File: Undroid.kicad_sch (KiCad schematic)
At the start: 36 parts, among them J1 AudioJack2, J2 JAE_SIM_Card_SF72S006, U1 ATSAME70J19A-AN, U2 AS4C256M16D3, U3 Allwinner-A13, U4 USR-C322

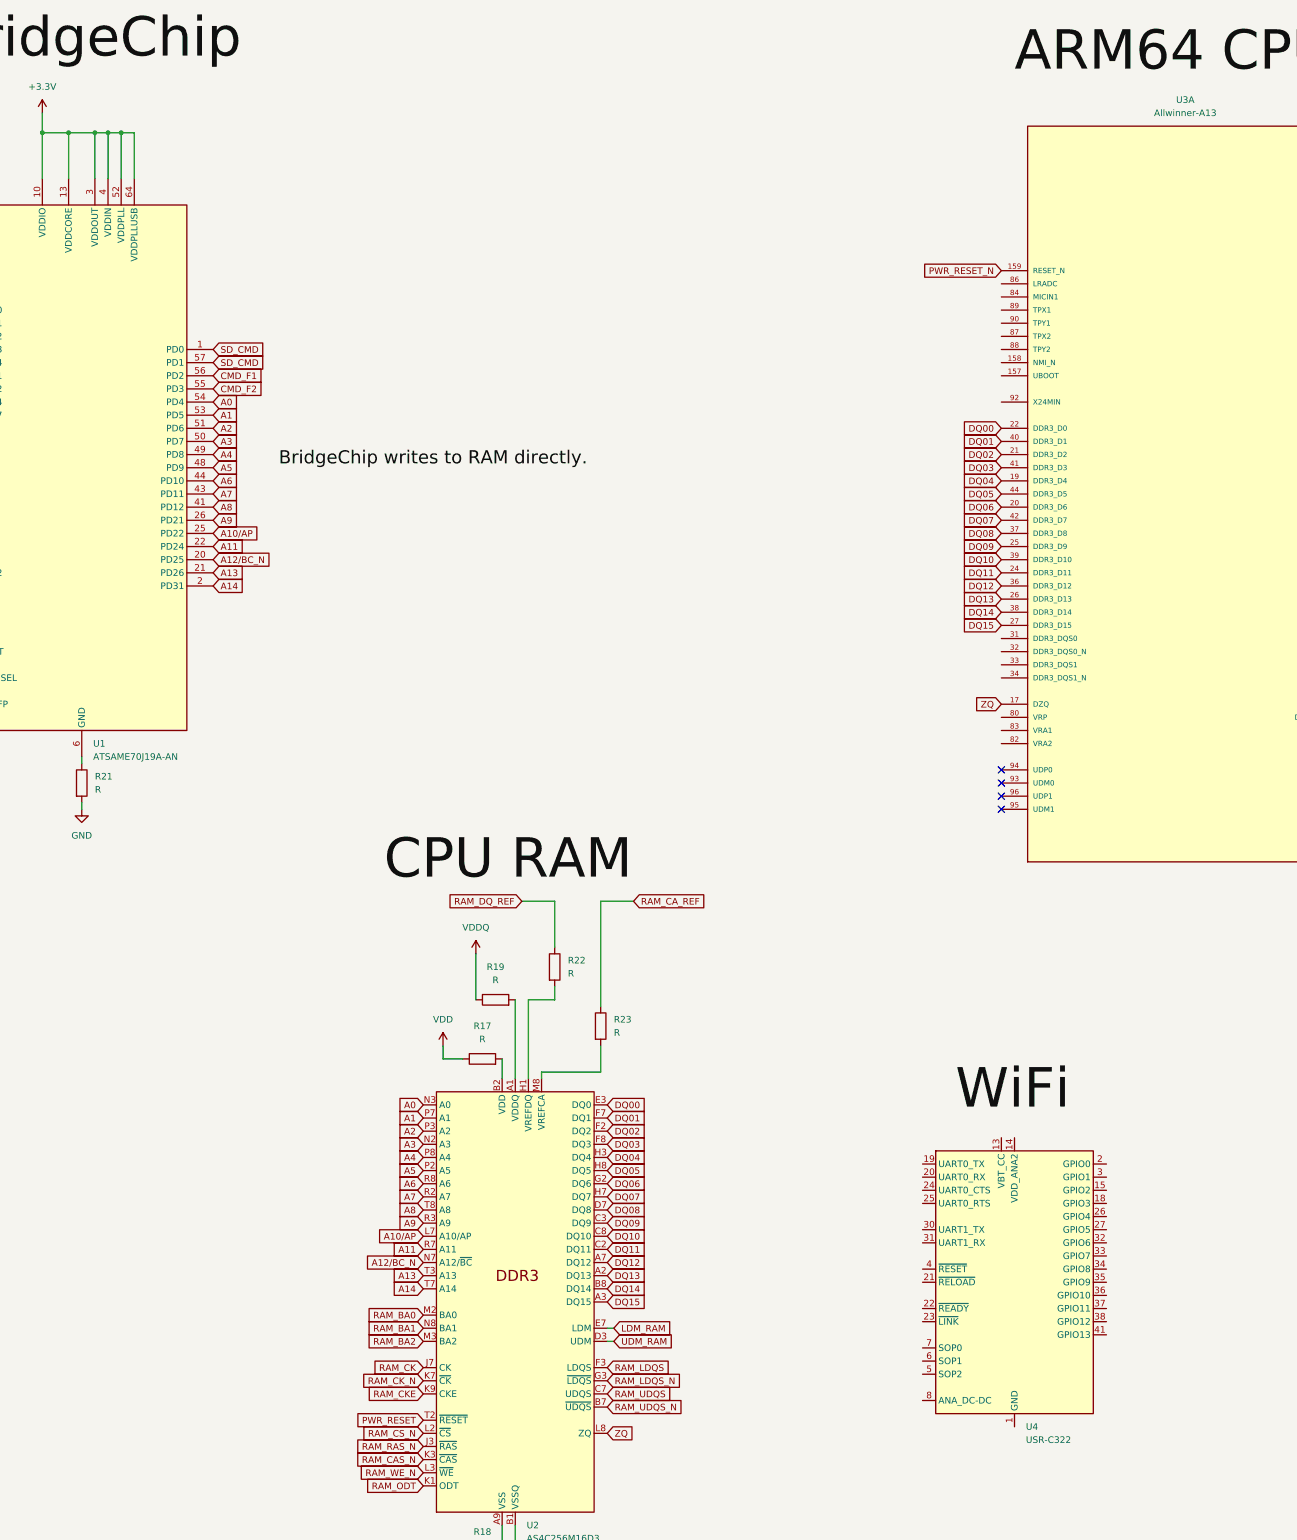
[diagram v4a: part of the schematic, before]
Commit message: main: Generate new pcb. Need to verify it.
Signed-off-by: Amlal EL Mahrouss <amlal@softwarelabs.com>
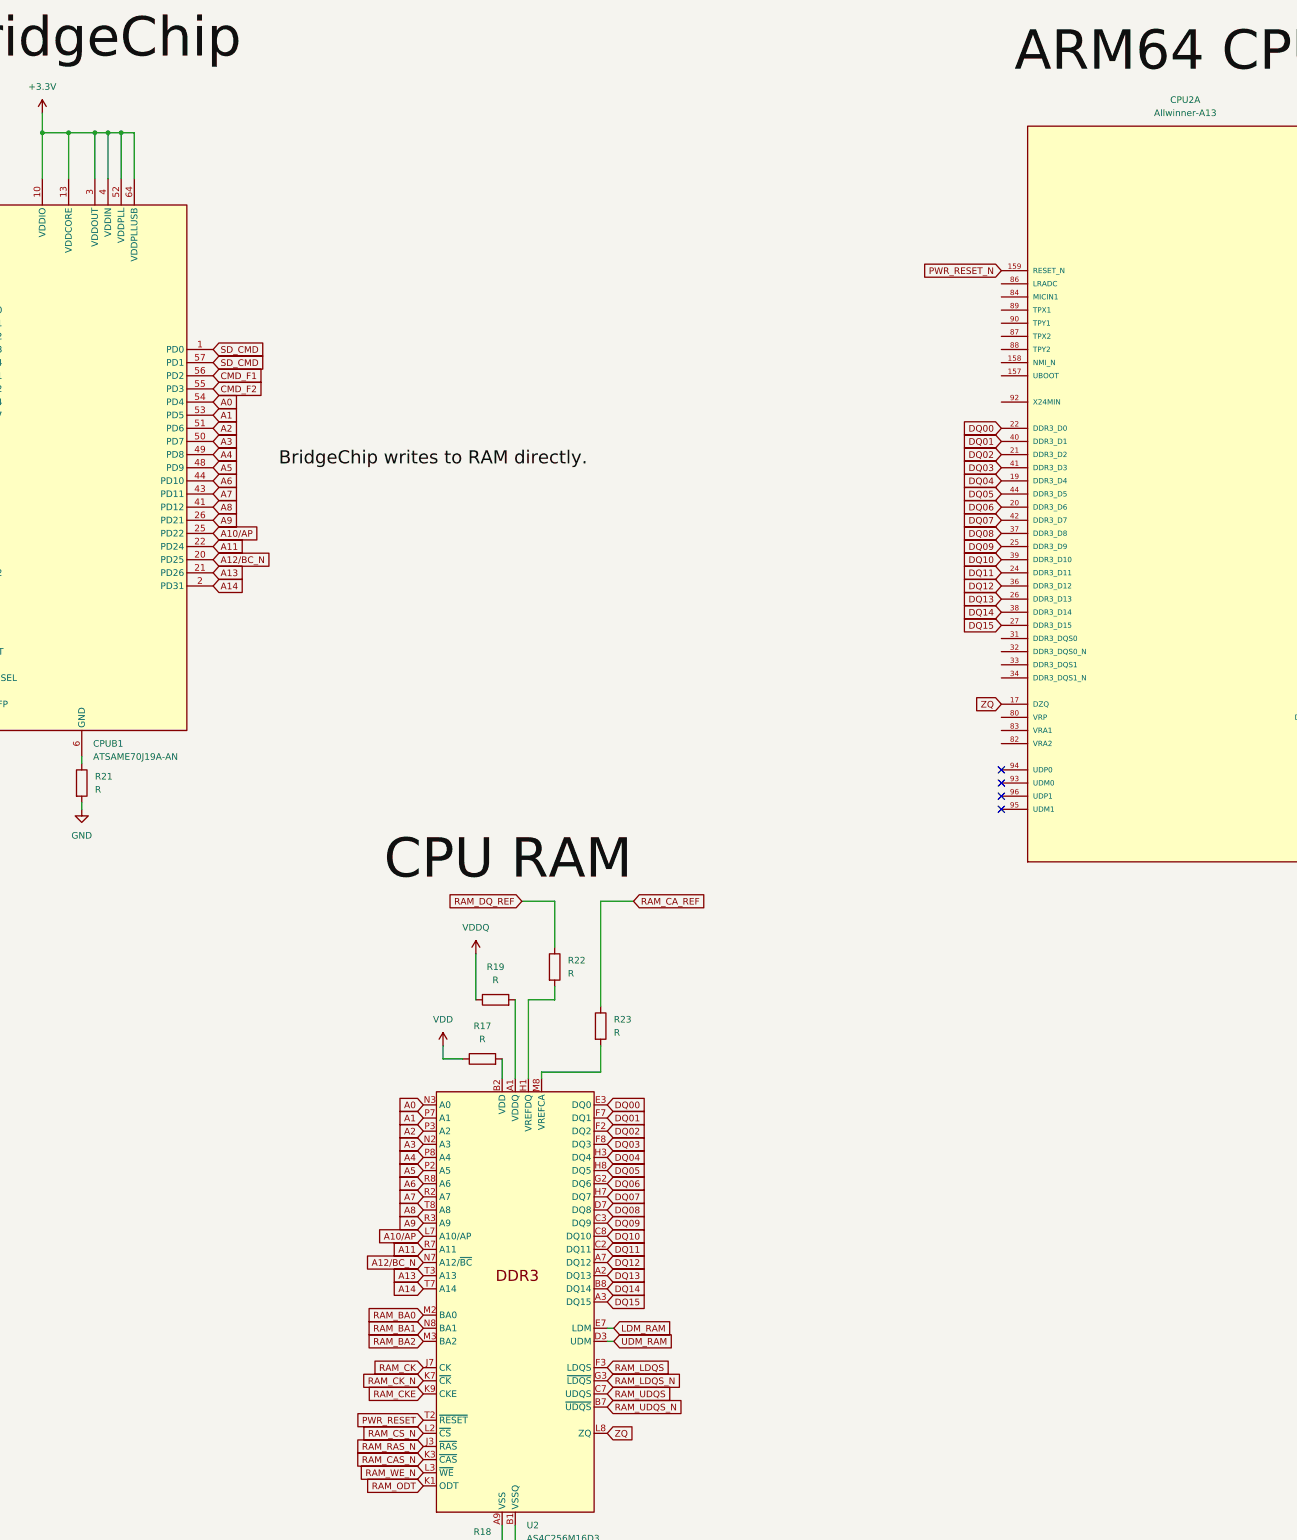
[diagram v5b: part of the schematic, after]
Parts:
- removed U4: USR-C322, RF_WiFi:USR-C322, symbol RF_WiFi:USR-C322
- CPU2: renamed from U3; footprint Allwinner-A13:QFP40P2200X2200X160-177N -> Allwinner:QFP40P2200X2200X160-177N
- renumbered U1 to CPUB1
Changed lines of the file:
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@@
 		)
 	)
-	(label "WiFi"
-		(at 463.55 278.13 0)
-		(fields_autoplaced yes)
-		(effects
-			(font
-				(size 7.62 7.62)
-			)
-			(justify left bottom)
-		)
-	)
 	(label "BridgeChip writes to RAM directly."
 		(at 332.74 152.4 0)
@@
 		(dnp no)
 		(fields_autoplaced yes)
-		(property "Reference" "U3"
+		(property "Reference" "CPU2"
 			(at 508 81.28 0)
 			(effects
@@
 			)
 		)
-		(property "Footprint" "Allwinner-A13:QFP40P2200X2200X160-177N"
+		(property "Footprint" "Allwinner:QFP40P2200X2200X160-177N"
 			(at 508 154.94 0)
 			(effects
@@
 			(project "Undroid"
 				(path "/5d3a3bfa-72d2-42b8-bac3-6ac6fe44d852"
-					(reference "U3")
+					(reference "CPU2")
 					(unit 1)
 				)
@@
 	)
 	(symbol
-		(lib_id "RF_WiFi:USR-C322")
-		(at 474.98 309.88 0)
-		(unit 1)
-		(exclude_from_sim no)
-		(in_bom yes)
-		(on_board yes)
-		(dnp no)
-		(fields_autoplaced yes)
-		(property "Reference" "U4"
-			(at 477.1741 337.82 0)
-			(effects
-				(font
-					(size 1.27 1.27)
-				)
-				(justify left)
-			)
-		)
-		(property "Value" "USR-C322"
-			(at 477.1741 340.36 0)
-			(effects
-				(font
-					(size 1.27 1.27)
-				)
-				(justify left)
-			)
-		)
-		(property "Footprint" "RF_WiFi:USR-C322"
-			(at 472.44 320.04 0)
-			(effects
-				(font
-					(size 1.27 1.27)
-				)
-				(hide yes)
-			)
-		)
-		(property "Datasheet" "https://www.usriot.com/download/WIFI/USR-C322%20User%20Manual%20V2.3.pdf"
-			(at 462.28 281.94 0)
-			(effects
-				(font
-					(size 1.27 1.27)
-				)
-				(hide yes)
-			)
-		)
-		(property "Description" "802.11 b/g/n Wi-Fi Module"
-			(at 474.98 309.88 0)
-			(effects
-				(font
-					(size 1.27 1.27)
-				)
-				(hide yes)
-			)
-		)
-		(pin "15"
-		)
-		(pin "16"
-		)
-		(pin "40"
-		)
-		(pin "13"
-		)
-		(pin "7"
-		)
-		(pin "22"
-		)
-		(pin "5"
-		)
-		(pin "1"
-		)
-		(pin "19"
-		)
-		(pin "11"
-		)
-		(pin "14"
-		)
-		(pin "17"
-		)
-		(pin "29"
-		)
-		(pin "28"
-		)
-		(pin "33"
-		)
-		(pin "38"
-		)
-		(pin "41"
-		)
-		(pin "8"
-		)
-		(pin "32"
-		)
-		(pin "26"
-		)
-		(pin "4"
-		)
-		(pin "21"
-		)
-		(pin "35"
-		)
-		(pin "31"
-		)
-		(pin "6"
-		)
-		(pin "42"
-		)
-		(pin "20"
-		)
-		(pin "12"
-		)
-		(pin "24"
-		)
-		(pin "39"
-		)
-		(pin "30"
-		)
-		(pin "25"
-		)
-		(pin "3"
-		)
-		(pin "10"
-		)
-		(pin "27"
-		)
-		(pin "34"
-		)
-		(pin "36"
-		)
-		(pin "44"
-		)
-		(pin "18"
-		)
-		(pin "23"
-		)
-		(pin "37"
-		)
-		(pin "43"
-		)
-		(pin "9"
-		)
-		(pin "2"
-		)
-		(instances
-			(project "Undroid"
-				(path "/5d3a3bfa-72d2-42b8-bac3-6ac6fe44d852"
-					(reference "U4")
-					(unit 1)
-				)
-			)
-		)
-	)
-	(symbol
 		(lib_id "Device:R")
 		(at 201.93 139.7 0)
@@
 		(dnp no)
 		(fields_autoplaced yes)
-		(property "Reference" "U1"
+		(property "Reference" "CPUB1"
 			(at 296.8341 205.74 0)
 			(effects
@@
 			(project "Undroid"
 				(path "/5d3a3bfa-72d2-42b8-bac3-6ac6fe44d852"
-					(reference "U1")
+					(reference "CPUB1")
 					(unit 1)
 				)

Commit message: main: new PCB.
Signed-off-by: Amlal EL Mahrouss <amlal@softwarelabs.com>
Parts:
- removed AE1: Antenna, RF_Antenna:Johanson_2450AT18x100, symbol Device:Antenna
- added AE1: Antenna_Shield, RF_Antenna:Texas_SWRA117D_2.4GHz_Right, symbol Device:Antenna_Shield
- added D1: LED, LED_SMD:LED_PLCC-2_3x2mm_AK, symbol Device:LED
- added J4: RFShield_OnePiece, RF_Shielding:Wuerth_36503205_20x20mm, symbol Device:RFShield_OnePiece
- added R10, R26, R27, R28, R29, R30, R31, R32: R, Resistor_SMD:R_0201_0603Metric, symbol Device:R
- renumbered PC1 to POWERC1
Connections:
- net CLK_F1 is gone; now on net RTC_OUT: FLASH1.3 (CLK)
- net CLK_F2 is gone; now on net RTC_OUT: FLASH2.3 (CLK)
- net +3.3V: now also CPU2.100 (VCC), CPU2.109 (VDD_INT), CPU2.11 (VDD_CPU), CPU2.142 (VCC), CPU2.149 (VDD_INT), CPU2.156 (VDD_CPU), CPU2.16 (VDD_CPU), CPU2.163 (VCC), CPU2.164 (VDD_CPU), CPU2.169 (VDD_CPU), CPU2.173 (VDD_CPU), CPU2.23 (VCC_DRAM), CPU2.30 (VCC_DRAM), CPU2.35 (VDD_INT), CPU2.4 (VDD_CPU), CPU2.43 (VCC_DRAM), CPU2.5 (VCC), CPU2.53 (VCC_DRAM), CPU2.62 (VCC_DRAM), CPU2.73 (VDD_INT), CPU2.81 (AVCC), CPU2.9 (VDD_CPU), CPU2.98 (VDD_INT), POWERC1.A9 (VBUS), POWERC1.B9 (VBUS); no longer R1.1
- net GND: now also CPU2.28 (DDR3_DM1), CPU2.29 (DDR3_DM0), CPU2.31 (DDR3_DQS0), CPU2.32 (DDR3_DQS0_N), CPU2.33 (DDR3_DQS1), CPU2.34 (DDR3_DQS1_N), CPU2.80 (VRP), CPU2.82 (VRA2), CPU2.83 (VRA1), CPU2.84 (MICIN1), CPU2.86 (LRADC), CPU2.87 (TPX2), CPU2.88 (TPY2), CPU2.89 (TPX1), CPU2.90 (TPY1), CPU2.93 (UDM0), CPU2.94 (UDP0), CPU2.95 (UDM1), CPU2.96 (UDP1), G1.11 (RTC_GPIO0), G1.12 (RTC_EINT), G1.24 (USB_VBUS), G1.25 (USB_DP), G1.26 (USB_DM), D1.1 (K), R10.1, R26.1, R27.1, R28.1, R29.1, R30.1, R31.1, R32.1; no longer CPUB1.38 (PB12), R15.1
- net GSM_STATUS: now also CPUB1.38 (PB12)
- net PWR_RESET: no longer U2.T2 (~{RESET})
- net RAM_BA0: now also CPU2.63 (DDR3_BA0)
- net RAM_BA1: now also CPU2.49 (DDR3_BA1)
- net RAM_BA2: now also CPU2.61 (DDR3_BA2)
- net RAM_CAS_N: now also CPU2.58 (DDR3_RAS)
- net RAM_CK: now also CPU2.45 (DDR3_CK)
- net RAM_CKE: now also CPU2.47 (DDR3_CKE)
- net RAM_CK_N: now also CPU2.46 (DDR3_CK_N)
- net RAM_ODT: now also CPU2.72 (DDR3_ODT)
- net RAM_RAS_N: now also CPU2.59 (DDR3_CAS)
- net RAM_WE_N: now also CPU2.60 (DDR3_WE)
- net at G1.32 (ANT): now also AE1.1 (A)
- net UBOOT: now reaches CPU2.157 (UBOOT)
- net NMI: now reaches CPU2.158 (NMI_N)
- net at CPU2.177 (GND): now also R16.2
- net at CPU2.18 (SVREF): now also R29.2
- net RAM_RST: now reaches CPU2.70 (DDR3_RST)
- net RAM_RST: now also U2.T2 (~{RESET})
- net at CPU2.74 (HPOUTL): now also R28.2
- net at CPU2.75 (HPBP): now also R27.2
- net at CPU2.76 (V33_HP): now also R30.2
- net at CPU2.77 (HPCOM): now also R26.2
- net at CPU2.78 (HPOUTR): now also R24.2
- net at CPU2.79 (AGND): now also R15.2
- net at CPU2.85 (VMIC): now also R32.2
- net RTC_OUT: now reaches CPU2.91 (X24MOUT)
- net RTC_OUT: now also J2.C3 (CLK), SD1.5 (CLK)
- net RTC_IN: now reaches CPU2.92 (X24MIN)
- net RTC_IN: now also G1.16 (SIM_CLK)
- net at CPU2.97 (V33_USB): now also R31.2
- net at POWERC1.A5 (CC1): now also R10.2; no longer R16.2
- net at POWERC1.B5 (CC2): now also R3.2; no longer R15.2
- net SHIELD: now reaches POWERC1.S1 (SHIELD)
- net SHIELD: now also SD1.9 (SHIELD), AE1.2 (Shield), J4.1 (Shield); no longer R3.2
- removed net GSM_CLK: G1.16 (SIM_CLK), J2.C3 (CLK), SD1.5 (CLK)
- net GSM_NET_LIGHT: no longer names the net of G1.41 (NETLIGHT)
- net GSM_NET_LIGHT: now also R1.2
- net GSM_SH: no longer names the net of J2.SH
- net PWR_RESET_N renamed PWR_RESET_BUT
- new net: D1.2 (A), R1.1
- new net GNDA: R15.1
- no-connect marks 9 -> 0
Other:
- moved on the sheet: R4, R5

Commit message: main: Reworking board now, because of Allwinner QFP package.
Signed-off-by: Amlal EL Mahrouss <amlal@softwarelabs.com>
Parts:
- added SHIELD_WUERTH1, SHIELD_WUERTH2: RFShield_OnePiece, RF_Shielding:Wuerth_36503205_20x20mm, symbol Device:RFShield_OnePiece
- renumbered J4 to SHIELD_WUERTH3
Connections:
- net SHIELD: no longer POWERC1.S1 (SHIELD), SD1.9 (SHIELD)
- new net: SD1.9 (SHIELD), SHIELD_WUERTH1.1 (Shield)
- new net: POWERC1.S1 (SHIELD), SHIELD_WUERTH2.1 (Shield)
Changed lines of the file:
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@@
 	(wire
 		(pts
-			(xy 561.34 96.52) (xy 543.56 96.52)
+			(xy 562.61 96.52) (xy 543.56 96.52)
 		)
 		(stroke
@@
 	(wire
 		(pts
-			(xy 561.34 93.98) (xy 561.34 96.52)
+			(xy 562.61 93.98) (xy 562.61 96.52)
 		)
 		(stroke
@@
 		)
 	)
+	(label "For Antenna"
+		(at 262.89 325.12 0)
+		(fields_autoplaced yes)
+		(effects
+			(font
+				(size 2.54 2.54)
+			)
+			(justify left bottom)
+		)
+	)
 	(label "BridgeChip writes to RAM directly."
 		(at 332.74 152.4 0)
@@
 		)
 	)
-	(global_label "SHIELD"
-		(shape input)
-		(at 209.55 170.18 270)
-		(fields_autoplaced yes)
-		(effects
-			(font
-				(size 1.27 1.27)
-			)
-			(justify right)
-		)
-		(property "Intersheetrefs" "${INTERSHEET_REFS}"
-			(at 209.55 179.7571 90)
-			(effects
-				(font
-					(size 1.27 1.27)
-				)
-				(justify right)
-				(hide yes)
-			)
-		)
-	)
 	(global_label "SD0_F1"
 		(shape input)
@@
 		)
 	)
-	(global_label "SHIELD"
-		(shape input)
-		(at 215.9 309.88 270)
-		(fields_autoplaced yes)
-		(effects
-			(font
-				(size 1.27 1.27)
-			)
-			(justify right)
-		)
-		(property "Intersheetrefs" "${INTERSHEET_REFS}"
-			(at 215.9 319.4571 90)
-			(effects
-				(font
-					(size 1.27 1.27)
-				)
-				(justify right)
-				(hide yes)
-			)
-		)
-	)
 	(global_label "SD_DAT1"
 		(shape input)
@@
 	)
 	(symbol
+		(lib_id "Device:RFShield_OnePiece")
+		(at 215.9 320.04 180)
+		(unit 1)
+		(exclude_from_sim no)
+		(in_bom yes)
+		(on_board yes)
+		(dnp no)
+		(fields_autoplaced yes)
+		(property "Reference" "SHIELD_WUERTH1"
+			(at 232.41 318.7699 0)
+			(effects
+				(font
+					(size 1.27 1.27)
+				)
+				(justify right)
+			)
+		)
+		(property "Value" "RFShield_OnePiece"
+			(at 232.41 321.3099 0)
+			(effects
+				(font
+					(size 1.27 1.27)
+				)
+				(justify right)
+			)
+		)
+		(property "Footprint" "RF_Shielding:Wuerth_36503205_20x20mm"
+			(at 215.9 317.5 0)
+			(effects
+				(font
+					(size 1.27 1.27)
+				)
+				(hide yes)
+			)
+		)
+		(property "Datasheet" "~"
+			(at 215.9 317.5 0)
+			(effects
+				(font
+					(size 1.27 1.27)
+				)
+				(hide yes)
+			)
+		)
+		(property "Description" "One-piece EMI RF shielding cabinet"
+			(at 215.9 320.04 0)
+			(effects
+				(font
+					(size 1.27 1.27)
+				)
+				(hide yes)
+			)
+		)
+		(pin "1"
+		)
+		(instances
+			(project "Undroid"
+				(path "/5d3a3bfa-72d2-42b8-bac3-6ac6fe44d852"
+					(reference "SHIELD_WUERTH1")
+					(unit 1)
+				)
+			)
+		)
+	)
+	(symbol
 		(lib_id "Device:R")
 		(at 374.65 255.27 90)
@@
 	)
 	(symbol
+		(lib_id "Device:RFShield_OnePiece")
+		(at 209.55 180.34 180)
+		(unit 1)
+		(exclude_from_sim no)
+		(in_bom yes)
+		(on_board yes)
+		(dnp no)
+		(fields_autoplaced yes)
+		(property "Reference" "SHIELD_WUERTH2"
+			(at 226.06 179.0699 0)
+			(effects
+				(font
+					(size 1.27 1.27)
+				)
+				(justify right)
+			)
+		)
+		(property "Value" "RFShield_OnePiece"
+			(at 226.06 181.6099 0)
+			(effects
+				(font
+					(size 1.27 1.27)
+				)
+				(justify right)
+			)
+		)
+		(property "Footprint" "RF_Shielding:Wuerth_36503205_20x20mm"
+			(at 209.55 177.8 0)
+			(effects
+				(font
+					(size 1.27 1.27)
+				)
+				(hide yes)
+			)
+		)
+		(property "Datasheet" "~"
+			(at 209.55 177.8 0)
+			(effects
+				(font
+					(size 1.27 1.27)
+				)
+				(hide yes)
+			)
+		)
+		(property "Description" "One-piece EMI RF shielding cabinet"
+			(at 209.55 180.34 0)
+			(effects
+				(font
+					(size 1.27 1.27)
+				)
+				(hide yes)
+			)
+		)
+		(pin "1"
+		)
+		(instances
+			(project "Undroid"
+				(path "/5d3a3bfa-72d2-42b8-bac3-6ac6fe44d852"
+					(reference "SHIELD_WUERTH2")
+					(unit 1)
+				)
+			)
+		)
+	)
+	(symbol
 		(lib_id "power:+3.3V")
 		(at 287.02 83.82 0)
@@
 	(symbol
 		(lib_id "power:+3.3V")
-		(at 561.34 93.98 0)
+		(at 562.61 93.98 0)
 		(unit 1)
 		(exclude_from_sim no)
@@
 		(fields_autoplaced yes)
 		(property "Reference" "#PWR057"
-			(at 561.34 97.79 0)
+			(at 562.61 97.79 0)
 			(effects
 				(font
@@
 		)
 		(property "Value" "+3.3V"
-			(at 561.34 88.9 0)
+			(at 562.61 88.9 0)
 			(effects
 				(font
@@
 		)
 		(property "Footprint" ""
-			(at 561.34 93.98 0)
+			(at 562.61 93.98 0)
 			(effects
 				(font
@@
 		)
 		(property "Datasheet" ""
-			(at 561.34 93.98 0)
+			(at 562.61 93.98 0)
 			(effects
 				(font
@@
 		)
 		(property "Description" "Power symbol creates a global label with name \"+3.3V\""
-			(at 561.34 93.98 0)
+			(at 562.61 93.98 0)
 			(effects
 				(font
@@
 		(dnp no)
 		(fields_autoplaced yes)
-		(property "Reference" "J4"
+		(property "Reference" "SHIELD_WUERTH3"
 			(at 279.4 347.9799 0)
 			(effects
@@
 			(project "Undroid"
 				(path "/5d3a3bfa-72d2-42b8-bac3-6ac6fe44d852"
-					(reference "J4")
+					(reference "SHIELD_WUERTH3")
 					(unit 1)
 				)

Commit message: main: Doing DRC and ERC right now...
Signed-off-by: Amlal EL Mahrouss <amlal@softwarelabs.com>
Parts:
- removed R15, R17, R24, R26, R27, R28, R29, R30, R31: R, Resistor_SMD:R_0201_0603Metric, symbol Device:R
- added R33: R, Resistor_SMD:R_0201_0603Metric, symbol Device:R
- added SHIELD_WUERTH4: RFShield_OnePiece, RF_Shielding:Wuerth_36503205_20x20mm, symbol Device:RFShield_OnePiece
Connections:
- net +1.8V is gone; now on net VDD: R7.2
- net GSM_PWR_MOD is gone; now on net GND: G1.39 (~{PWRKEY})
- net PWR_RESET_BUT is gone; now on net RESET: CPU2.159 (RESET_N)
- net +3.3V: now also R6.1, R8.1; no longer J2.C1 (VCC), POWERC1.A9 (VBUS), POWERC1.B9 (VBUS), R11.2, R12.1, R13.2, R4.2, R6.2, R8.2
- net GND: no longer CPU2.28 (DDR3_DM1), CPU2.29 (DDR3_DM0), CPU2.31 (DDR3_DQS0), CPU2.32 (DDR3_DQS0_N), CPU2.33 (DDR3_DQS1), CPU2.34 (DDR3_DQS1_N), CPU2.80 (VRP), CPU2.82 (VRA2), CPU2.83 (VRA1), CPU2.93 (UDM0), CPU2.94 (UDP0), CPU2.95 (UDM1), CPU2.96 (UDP1), CPUB1.59 (DM), CPUB1.60 (DP), G1.11 (RTC_GPIO0), G1.25 (USB_DP), G1.26 (USB_DM)
- net RAM_LDQS: now also CPU2.33 (DDR3_DQS1)
- net RAM_LDQS_N: now also CPU2.34 (DDR3_DQS1_N)
- net RAM_UDQS: now also CPU2.31 (DDR3_DQS0)
- net RAM_UDQS_N: now also CPU2.32 (DDR3_DQS0_N)
- net at CPU2.76 (V33_HP): now also CPU2.18 (SVREF), CPU2.85 (VMIC), CPU2.97 (V33_USB), R32.2
- net at U2.B2 (VDD), U2.D9 (VDD), U2.G7 (VDD)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: now also R7.1
- net at FLASH2.8 (VDD): now also R11.2; no longer R11.1
- net at G1.40 (VDD_EXT): no longer R7.1
- net at G1.9 (VDD_3V3): now also R6.2; no longer R6.1
- net at G1.34 (VBAT), G1.35 (VBAT): now also R8.2; no longer R8.1
- net at J2.SH: now also SHIELD_WUERTH4.1 (Shield)
- net GSM_CSW: no longer names the net of J2.CSW
- net GSM_DSW: no longer names the net of J2.DSW
- net GSM_GEN: no longer names the net of G1.18 (SIM_VDD)
- net GSM_RST_MOD: no longer names the net of G1.28 (~{RESET})
- net NMI: no longer names the net of CPU2.158 (NMI_N)
- net PWR_RESET renamed RESET
- net RAM_CA_REF renamed VREFCA
- net RAM_DQ_REF renamed VREFDQ
- net VDDQ renamed VBUS_USBC
- net VBUS_USBC: now also POWERC1.A9 (VBUS), POWERC1.B9 (VBUS), R11.1, R12.1, R13.2, R4.2, R33.2
- new net: J2.C1 (VCC), R33.1
- no-connect marks 0 -> 25
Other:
- note added: "ARM CPU"
- note added: "Bridge MCU"
- note added: "DDR3 RAM"
- note added: "GPRS modem"
- note added: "Memory (SIM, Flash, SD)"
- note added: "Power Line"
- note added: "TODO: Unit 2 Allwinner"
- note added: "The board also contains EMI shields. for Antennas, SIM, SD, Power..."
- moved on the sheet: R11, R18, R21, R6, R8
